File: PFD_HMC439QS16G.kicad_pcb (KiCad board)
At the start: 2 copper layers, 160 x 100 mm, 85 parts, among them J1 REF, J2 IN, J3 Error_Out, J4 C64AC, J5 Switch, J6 Fast_Out, U1 HMC439QS16G, U2 LT3045EMSE, U3 LT3094EMSE, U4 ADA4896-2ARMZ, U5 ADA4896-2ARMZ, U6 HMC365S8G, U7 L7808, U8 ADG1413, U9 LTC6228xS8

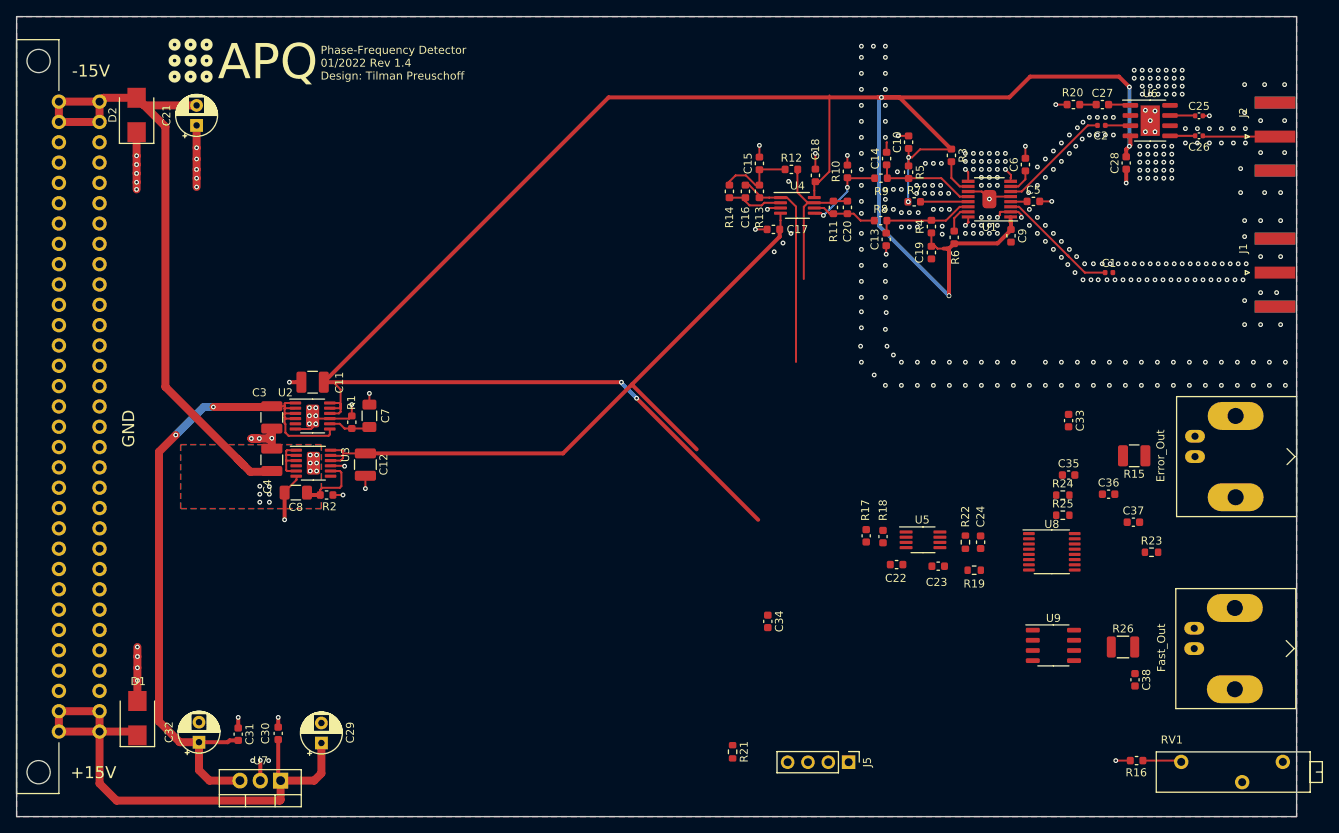
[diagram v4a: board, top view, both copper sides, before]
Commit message: Add fast PD regulator
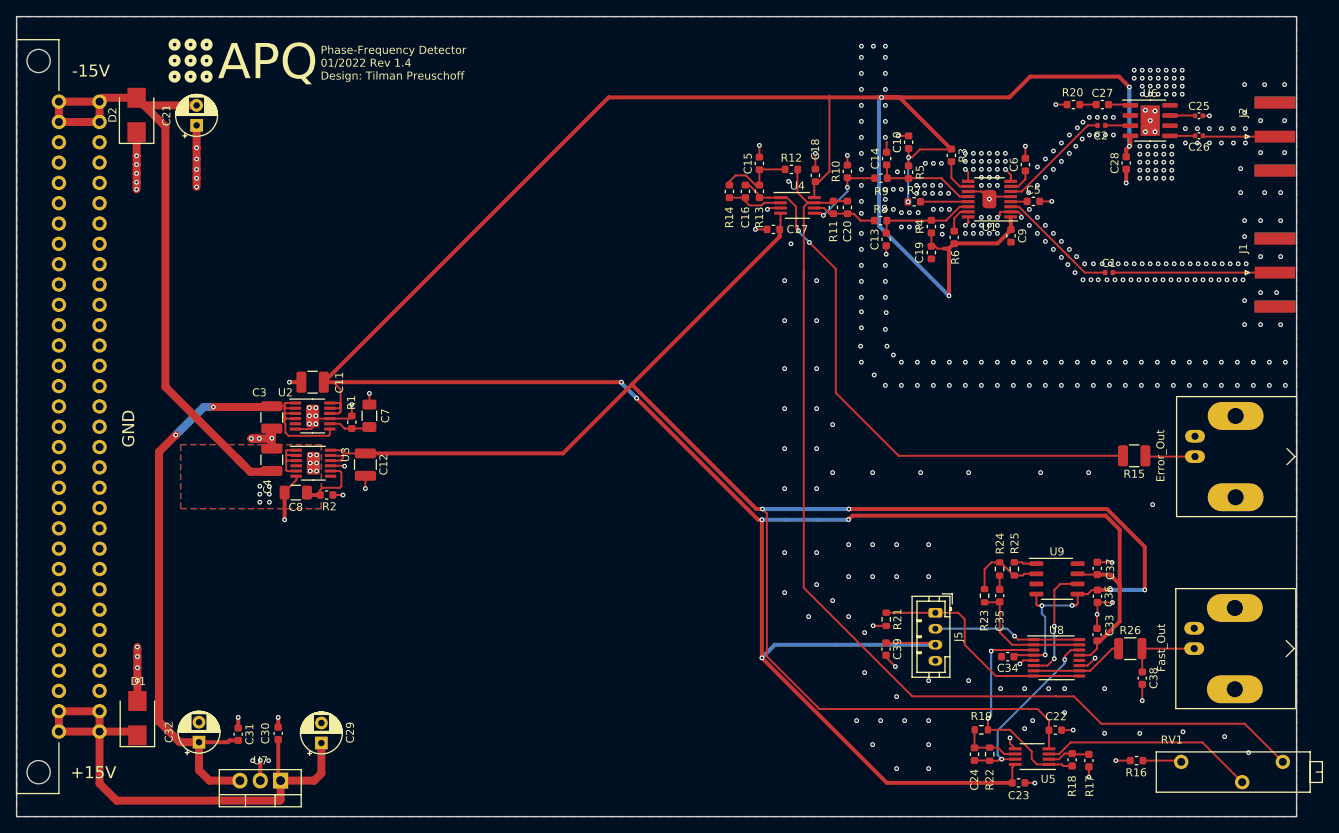
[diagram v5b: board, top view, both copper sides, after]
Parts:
- added C39: 100n, Capacitor_SMD:C_0603_1608Metric, F.Cu at (178.7, 129.1)
- J5: footprint Connector_PinHeader_2.54mm:PinHeader_1x04_P2.54mm_Vertical -> Connector_JST:JST_PH_B4B-PH-K_1x04_P2.00mm_Vertical
- moved R17 39.6 mm to (204.0, 143.0), turned to 270 degrees
- moved R18 36.6 mm to (201.9, 142.9), turned to 90 degrees
- moved U5 30.3 mm to (196.9, 142.5), turned to 180 degrees
- moved C34 30.3 mm to (193.9, 130.0), turned to 180 degrees
- moved C23 28.9 mm to (195.2, 145.8), turned to 0 degrees
- moved C22 28.7 mm to (199.8, 139.2), turned to 0 degrees
- moved C33 27.0 mm to (205.1, 127.3), turned to 90 degrees
- moved R22 26.7 mm to (191.6, 142.2), turned to 270 degrees
- moved C24 26.5 mm to (189.7, 142.2), turned to 90 degrees
- moved R21 25.4 mm to (178.7, 125.3)
- moved J5 21.6 mm to (184.8, 124.5)
- moved R23 21.6 mm to (191.0, 122.4), turned to 90 degrees
- moved R19 20.0 mm to (190.6, 139.2), turned to 180 degrees
- moved C35 17.4 mm to (192.9, 122.4), turned to 270 degrees
- moved U8 13.3 mm to (200.0, 130.1)
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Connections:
- J4 pad A10: (no net) -> Net-(J4-PadA10)
- J4 pad A11: (no net) -> Net-(J4-PadA11)
- J4 pad A12: (no net) -> Net-(J4-PadA12)
- J4 pad A13: (no net) -> Net-(J4-PadA13)
- J4 pad A14: (no net) -> Net-(J4-PadA14)
- J4 pad A19: (no net) -> Net-(J4-PadA19)
- J4 pad A20: (no net) -> Net-(J4-PadA20)
- J4 pad A21: (no net) -> Net-(J4-PadA21)
- J4 pad A22: (no net) -> Net-(J4-PadA22)
- J4 pad A23: (no net) -> Net-(J4-PadA23)
- J4 pad A24: (no net) -> Net-(J4-PadA24)
- J4 pad A25: (no net) -> Net-(J4-PadA25)
- J4 pad A26: (no net) -> Net-(J4-PadA26)
- J4 pad A27: (no net) -> Net-(J4-PadA27)
- J4 pad A28: (no net) -> Net-(J4-PadA28)
- J4 pad A29: (no net) -> Net-(J4-PadA29)
- J4 pad A3: (no net) -> Net-(J4-PadA3)
- J4 pad A30: (no net) -> Net-(J4-PadA30)
- J4 pad A4: (no net) -> Net-(J4-PadA4)
- J4 pad A5: (no net) -> Net-(J4-PadA5)
- J4 pad A6: (no net) -> Net-(J4-PadA6)
- J4 pad A7: (no net) -> Net-(J4-PadA7)
- J4 pad A8: (no net) -> Net-(J4-PadA8)
- J4 pad A9: (no net) -> Net-(J4-PadA9)
- J4 pad C10: (no net) -> Net-(J4-PadC10)
- J4 pad C11: (no net) -> Net-(J4-PadC11)
- J4 pad C12: (no net) -> Net-(J4-PadC12)
- J4 pad C13: (no net) -> Net-(J4-PadC13)
- J4 pad C14: (no net) -> Net-(J4-PadC14)
- J4 pad C19: (no net) -> Net-(J4-PadC19)
- J4 pad C20: (no net) -> Net-(J4-PadC20)
- J4 pad C21: (no net) -> Net-(J4-PadC21)
- J4 pad C22: (no net) -> Net-(J4-PadC22)
- J4 pad C23: (no net) -> Net-(J4-PadC23)
- J4 pad C24: (no net) -> Net-(J4-PadC24)
- J4 pad C25: (no net) -> Net-(J4-PadC25)
- J4 pad C26: (no net) -> Net-(J4-PadC26)
- J4 pad C27: (no net) -> Net-(J4-PadC27)
- J4 pad C28: (no net) -> Net-(J4-PadC28)
- J4 pad C29: (no net) -> Net-(J4-PadC29)
- J4 pad C3: (no net) -> Net-(J4-PadC3)
- J4 pad C30: (no net) -> Net-(J4-PadC30)
- J4 pad C4: (no net) -> Net-(J4-PadC4)
- J4 pad C5: (no net) -> Net-(J4-PadC5)
- J4 pad C6: (no net) -> Net-(J4-PadC6)
- J4 pad C7: (no net) -> Net-(J4-PadC7)
- J4 pad C8: (no net) -> Net-(J4-PadC8)
- J4 pad C9: (no net) -> Net-(J4-PadC9)
- U2 pad 5: (no net) -> Net-(U2-Pad5)
- U3 pad 4: (no net) -> Net-(U3-Pad4)
- U3 pad 7: (no net) -> Net-(U3-Pad7)
- U9 pad 8: (no net) -> Net-(U9-Pad8)
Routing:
- net +5V: track 287.8 -> 445.7 mm, vias 8 -> 11
- net -5V: track 86.0 -> 240.7 mm, vias 0 -> 7
- net /Fast PD regulator/error_sig: track 19.5 -> 128.0 mm
- net Net-(C16-Pad1): track 27.0 -> 72.1 mm, vias 0 -> 2
- net Net-(J5-Pad1): track 0.00 -> 29.3 mm
- net S1: track 0.00 -> 28.3 mm, vias 0 -> 2
- net Net-(RV1-Pad2): track 0.00 -> 26.8 mm
- net S2: track 0.00 -> 23.9 mm, vias 0 -> 2
- net GND: track 99.5 -> 122.0 mm, vias 378 -> 451
- net Net-(C1-Pad2): track 0.00 -> 20.3 mm
- net Net-(J5-Pad2): track 0.00 -> 18.6 mm, vias 0 -> 1
- net D1D2: track 0.00 -> 16.3 mm
- net S4: track 0.00 -> 15.5 mm, vias 0 -> 2
- net D4: track 0.00 -> 11.8 mm
- net Net-(R23-Pad2): track 0.00 -> 10.1 mm
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
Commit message: Add 'no divider' option and clamping diode / Update to KiCad 6
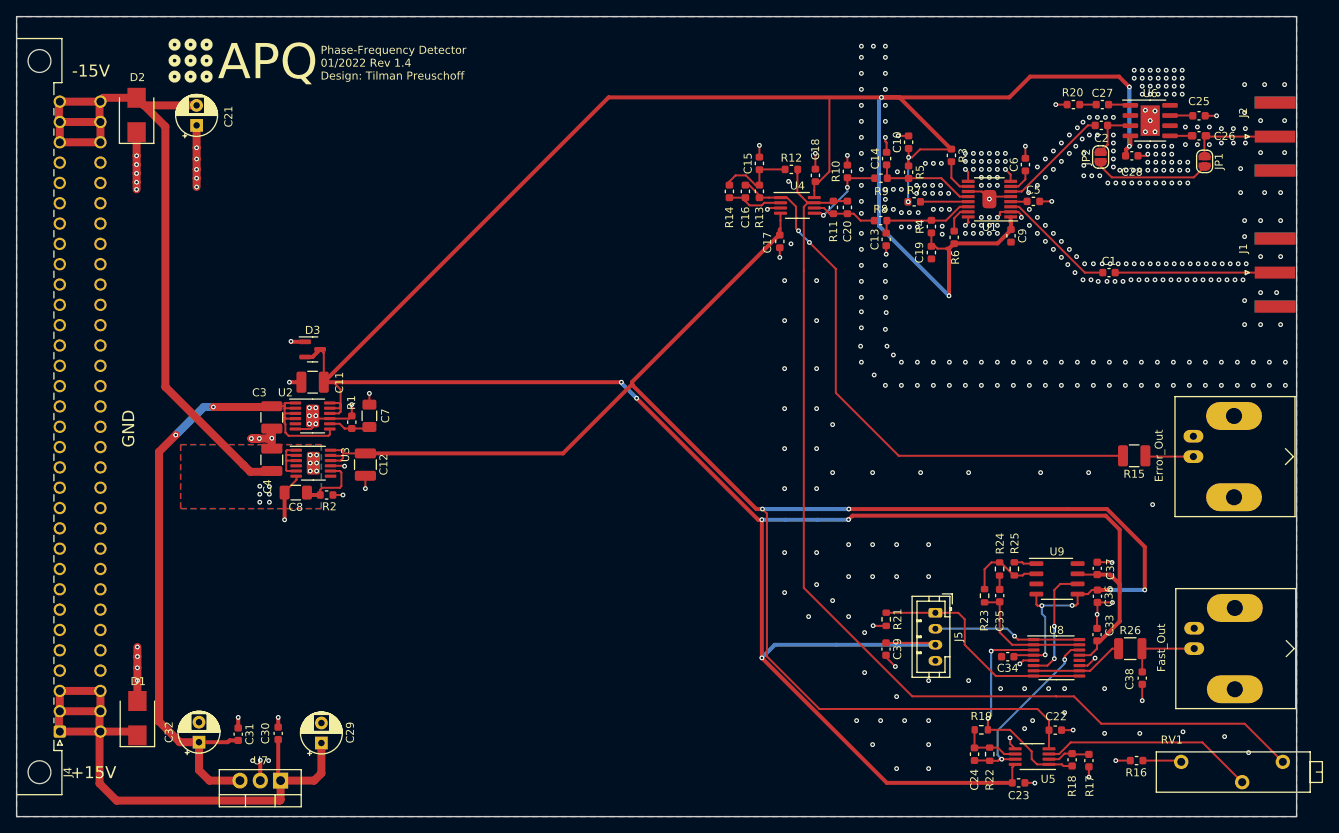
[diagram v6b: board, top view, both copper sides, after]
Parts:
- added D3: PMEG2010, Package_TO_SOT_SMD:SOT-23, F.Cu at (107.0, 91.6)
- added JP1: no_divider, Jumper:SolderJumper-2_P1.3mm_Open_RoundedPad1.0x1.5mm, F.Cu at (218.5, 68.1)
- added JP2: no_divider, Jumper:SolderJumper-2_P1.3mm_Open_RoundedPad1.0x1.5mm, F.Cu at (205.5, 67.5)
- C1, C2, C25: footprint Capacitor_SMD:C_0402_1005Metric -> Capacitor_SMD:C_0603_1608Metric
- C26: footprint Capacitor_SMD:C_0402_1005Metric -> Capacitor_SMD:C_0603_1608Metric_Pad1.08x0.95mm_HandSolder
- J4: footprint footprints:Socket_DIN41612-CaseC1-AC-Male-64Pin-2rows -> Connector_DIN:DIN41612_C_2x32_Male_Horizontal_THT
- moved J4 39.4 mm to (75.4, 139.4), turned to 90 degrees
- moved C17 1.70 mm to (165.4, 78.1), turned to -90 degrees
- moved C28 1.14 mm to (209.4, 67.4), turned to 180 degrees
- moved J3 0.20 mm to (217.1, 105.0)
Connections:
- U2 pad 5: Net-(U2-Pad5) -> unconnected-(U2-Pad5)
- U3 pad 4: Net-(U3-Pad4) -> unconnected-(U3-Pad4)
- U3 pad 7: Net-(U3-Pad7) -> unconnected-(U3-Pad7)
- U9 pad 8: Net-(U9-Pad8) -> unconnected-(U9-Pad8)
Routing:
- net Net-(JP2-Pad1): track 0.00 -> 14.6 mm
- net +15V: track 67.1 -> 77.3 mm
- net IN: track 91.8 -> 100.9 mm
- net +5V: track 445.7 -> 450.5 mm
- net Div_out: track 3.17 -> 6.74 mm
- net GND: track 122.0 -> 124.4 mm, vias 451 -> 470
- net Net-(JP1-Pad1): track 9.06 -> 11.3 mm
- net -5V: track 240.7 -> 239.0 mm
- net /Fast PD regulator/error_sig: track 128.0 -> 127.0 mm
- net S4: track 15.5 -> 14.8 mm
- net Net-(C1-Pad1): track 15.5 -> 14.9 mm
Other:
- net class Default removed

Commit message: Fix HMC365 and ADG1413 symbols. Update gerber files.
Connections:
- U6 pad 2: (no net) -> unconnected-(U6-Pad2)
- U6 pad 6: (no net) -> unconnected-(U6-Pad6)
- U8 pad 12: (no net) -> unconnected-(U8-Pad12)
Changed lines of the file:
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@@
   (net 92 "unconnected-(J4-Padc28)")
   (net 93 "unconnected-(J4-Padc29)")
-  (net 94 "Net-(JP1-Pad1)")
-  (net 95 "Net-(JP2-Pad1)")
+  (net 94 "Net-(C26-Pad2)")
+  (net 95 "Net-(JP1-Pad2)")
+  (net 96 "unconnected-(U8-Pad12)")
+  (net 97 "unconnected-(U6-Pad2)")
+  (net 98 "unconnected-(U6-Pad6)")
   (footprint "Capacitor_SMD:C_0603_1608Metric" (layer "F.Cu")
     (at 205.6 63.6)
@@
       (net 27 "Net-(C26-Pad1)") (pintype "passive"))
     (pad "2" smd roundrect (at 0.8625 0) (size 1.075 0.95) (layers "F.Cu" "F.Paste" "F.Mask") (roundrect_rratio 0.25)
-      (net 94 "Net-(JP1-Pad1)") (pintype "passive"))
+      (net 94 "Net-(C26-Pad2)") (pintype "passive"))
     (model "${KICAD6_3DMODEL_DIR}/Capacitor_SMD.3dshapes/C_0603_1608Metric.wrl"
       (offset (xyz 0 0 0))
@@
     (pad "1" smd roundrect locked (at -2.475 -1.905) (size 1.95 0.6) (layers "F.Cu" "F.Paste" "F.Mask") (roundrect_rratio 0.25)
       (net 28 "Net-(C27-Pad2)") (pinfunction "~{OUT}") (pintype "output"))
-    (pad "2" smd roundrect locked (at -2.475 -0.635) (size 1.95 0.6) (layers "F.Cu" "F.Paste" "F.Mask") (roundrect_rratio 0.25))
+    (pad "2" smd roundrect locked (at -2.475 -0.635) (size 1.95 0.6) (layers "F.Cu" "F.Paste" "F.Mask") (roundrect_rratio 0.25)
+      (net 97 "unconnected-(U6-Pad2)") (pinfunction "NC") (pintype "no_connect"))
     (pad "3" smd roundrect locked (at -2.475 0.635) (size 1.95 0.6) (layers "F.Cu" "F.Paste" "F.Mask") (roundrect_rratio 0.25)
       (net 25 "Div_out") (pinfunction "OUT") (pintype "output"))
@@
     (pad "5" smd roundrect locked (at 2.475 1.905) (size 1.95 0.6) (layers "F.Cu" "F.Paste" "F.Mask") (roundrect_rratio 0.25)
       (net 27 "Net-(C26-Pad1)") (pinfunction "IN") (pintype "input"))
-    (pad "6" smd roundrect locked (at 2.475 0.635) (size 1.95 0.6) (layers "F.Cu" "F.Paste" "F.Mask") (roundrect_rratio 0.25))
+    (pad "6" smd roundrect locked (at 2.475 0.635) (size 1.95 0.6) (layers "F.Cu" "F.Paste" "F.Mask") (roundrect_rratio 0.25)
+      (net 98 "unconnected-(U6-Pad6)") (pinfunction "NC") (pintype "no_connect"))
     (pad "7" smd roundrect locked (at 2.475 -0.635) (size 1.95 0.6) (layers "F.Cu" "F.Paste" "F.Mask") (roundrect_rratio 0.25)
       (net 26 "Net-(C25-Pad2)") (pinfunction "~{IN}") (pintype "input"))
@@
     (pad "11" smd roundrect locked (at 2.8625 0.975) (size 1.475 0.4) (layers "F.Cu" "F.Paste" "F.Mask") (roundrect_rratio 0.25)
       (net 4 "GND") (pinfunction "S3") (pintype "bidirectional"))
-    (pad "12" smd roundrect locked (at 2.8625 0.325) (size 1.475 0.4) (layers "F.Cu" "F.Paste" "F.Mask") (roundrect_rratio 0.25))
+    (pad "12" smd roundrect locked (at 2.8625 0.325) (size 1.475 0.4) (layers "F.Cu" "F.Paste" "F.Mask") (roundrect_rratio 0.25)
+      (net 96 "unconnected-(U8-Pad12)") (pinfunction "NC") (pintype "no_connect"))
     (pad "13" smd roundrect locked (at 2.8625 -0.325) (size 1.475 0.4) (layers "F.Cu" "F.Paste" "F.Mask") (roundrect_rratio 0.25)
       (net 9 "+5V") (pinfunction "Vdd") (pintype "power_in"))
@@
     (fp_line (start -1.91 -5.08) (end 4.445 -5.08) (layer "F.Fab") (width 0.1))
     (pad "1" smd rect locked (at 0 0 90) (size 1.5 5.08) (layers "F.Cu" "F.Paste" "F.Mask")
-      (net 94 "Net-(JP1-Pad1)") (pinfunction "In") (pintype "passive"))
+      (net 94 "Net-(C26-Pad2)") (pinfunction "In") (pintype "passive"))
     (pad "2" smd rect locked (at 0 4.25 90) (size 1.5 5.08) (layers "F.Cu" "F.Paste" "F.Mask")
       (net 4 "GND") (pinfunction "Ext") (pintype "passive"))
@@
     (fp_line (start -1.65 -1.25) (end -1.65 1.25) (layer "F.CrtYd") (width 0.05))
     (pad "1" smd custom (at -0.65 0 90) (size 1 0.5) (layers "F.Cu" "F.Mask")
-      (net 95 "Net-(JP2-Pad1)") (pinfunction "A") (pintype "passive") (zone_connect 2)
+      (net 95 "Net-(JP1-Pad2)") (pinfunction "A") (pintype "passive") (zone_connect 2)
       (options (clearance outline) (anchor rect))
       (primitives
@@
     (fp_line (start -1.65 -1.25) (end 1.65 -1.25) (layer "F.CrtYd") (width 0.05))
     (pad "1" smd custom (at -0.65 0 270) (size 1 0.5) (layers "F.Cu" "F.Mask")
-      (net 94 "Net-(JP1-Pad1)") (pinfunction "A") (pintype "passive") (zone_connect 2)
+      (net 94 "Net-(C26-Pad2)") (pinfunction "A") (pintype "passive") (zone_connect 2)
       (options (clearance outline) (anchor rect))
       (primitives
@@
       ))
     (pad "2" smd custom (at 0.65 0 270) (size 1 0.5) (layers "F.Cu" "F.Mask")
-      (net 95 "Net-(JP2-Pad1)") (pinfunction "B") (pintype "passive") (zone_connect 2)
+      (net 95 "Net-(JP1-Pad2)") (pinfunction "B") (pintype "passive") (zone_connect 2)
       (options (clearance outline) (anchor rect))
       (primitives

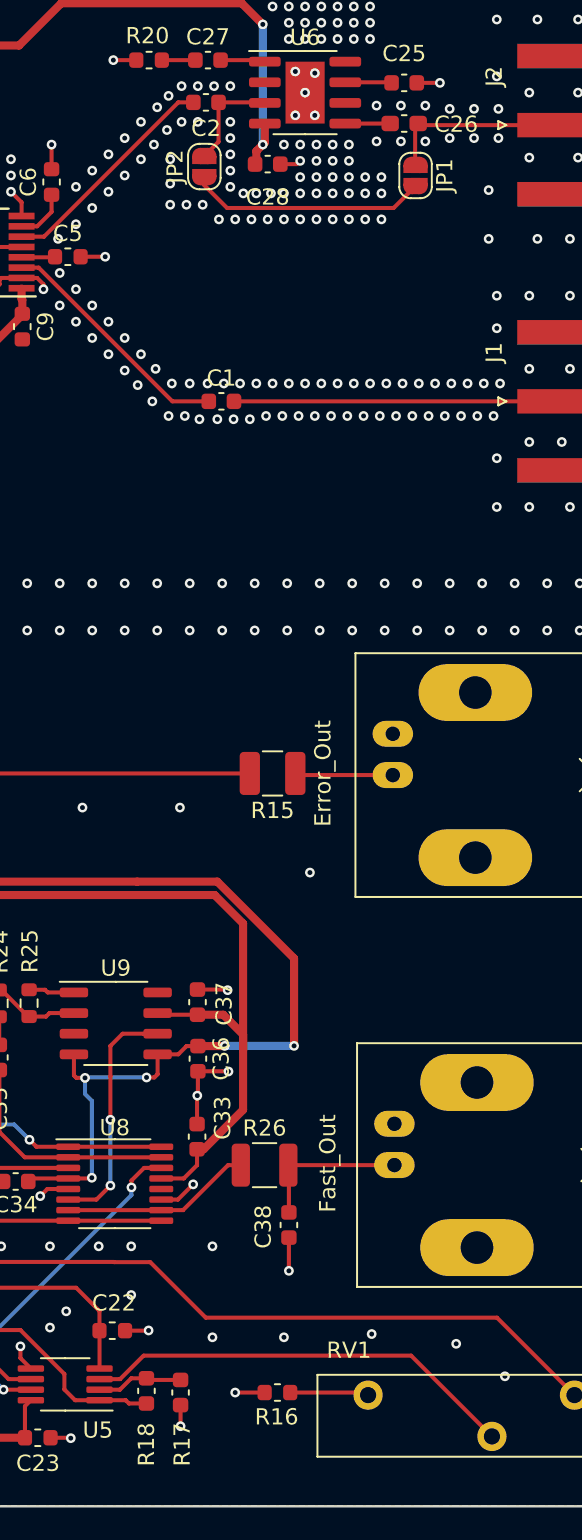
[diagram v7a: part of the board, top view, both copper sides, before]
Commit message: Update BOM / fix some fottprints
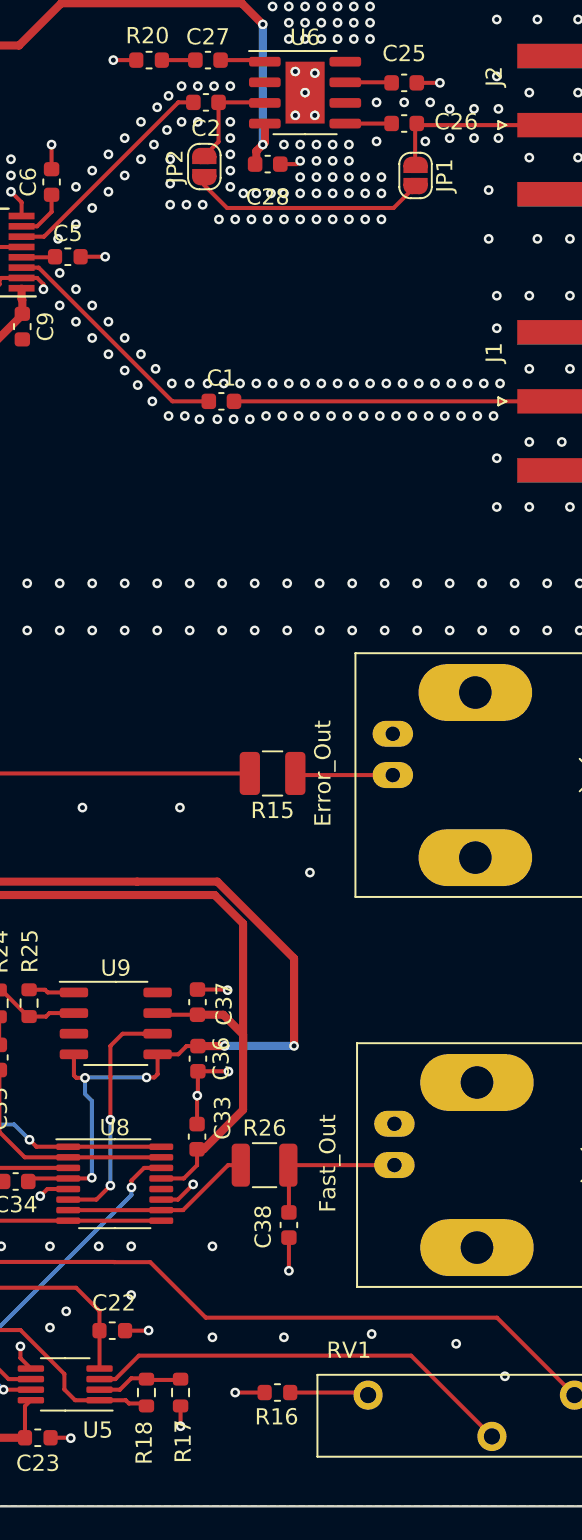
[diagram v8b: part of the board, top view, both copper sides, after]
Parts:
- C16: value 140p -> 150p
- C26: footprint Capacitor_SMD:C_0603_1608Metric_Pad1.08x0.95mm_HandSolder -> Capacitor_SMD:C_0603_1608Metric
- C7, C8: value 0.47u -> 100n
- R10, R11: value 380 -> 390
- R16: value 10 -> 20
- R17, R18: footprint Capacitor_SMD:C_0603_1608Metric -> Resistor_SMD:R_0603_1608Metric
- U8: value ADG1413 -> ADG1613
- moved R18 0.10 mm to (201.9, 143.0)
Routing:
- net GND: vias 470 -> 469
